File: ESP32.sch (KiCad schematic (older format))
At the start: 15 parts, among them J201 Conn_01x20, J202 Conn_01x20, U201 ESP32-WROOM-32D

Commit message: Rough PCB layout
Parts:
- removed J201, J202: Conn_01x20, symbol Connector_Generic:Conn_01x20
- added C203: 100nF, Capacitor_SMD:C_0402_1005Metric, symbol Device:C
- added J201: Conn_02x13_Odd_Even, Connector_PinHeader_2.54mm:PinHeader_2x13_P2.54mm_Vertical, symbol Connector_Generic:Conn_02x13_Odd_Even
- added J202: Conn_02x10_Odd_Even, Connector_PinHeader_2.54mm:PinHeader_2x10_P2.54mm_Vertical, symbol Connector_Generic:Conn_02x10_Odd_Even
- added J203: Conn_01x02, Connector_PinHeader_2.54mm:PinHeader_1x02_P2.54mm_Vertical, symbol Connector_Generic:Conn_01x02
- added R211, R212: 1k, Resistor_SMD:R_0402_1005Metric, symbol Device:R
- C201: value 100n -> 100nF; footprint (none) -> Capacitor_SMD:C_0402_1005Metric
- C202: footprint Capacitor_SMD:C_0805_2012Metric -> Capacitor_SMD:C_0603_1608Metric
- R201: footprint (none) -> Resistor_SMD:R_0402_1005Metric
- R202, R203, R204, R205, R206, R207, R208, R209, R210: footprint (none) -> Resistor_SMD:R_0603_1608Metric
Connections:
- net labels added: USB_5V
- net labels removed: EXT_5V, SCK, SCS, SDI, SDO, SHD, SWP
- wire segments 45 -> 53
- no-connect marks 0 -> 6
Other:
- moved on the sheet: C202, R201, U201

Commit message: Specified JLCPCB footprints for components
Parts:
- C201, C203: LCSC (none) -> C1525
- C202: LCSC C45783 -> C59461
- J201: LCSC (none) -> C358701
- J202: LCSC (none) -> C358699
- J203: LCSC (none) -> C376075
- R201: LCSC (none) -> C25744
- R202, R203, R204, R205, R206, R207, R208, R209, R210: LCSC (none) -> C21189
- R211, R212: LCSC (none) -> C11702
- U201: LCSC (none) -> C82899
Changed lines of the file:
@@
 F 2 "RF_Module:ESP32-WROOM-32" H 3700 1750 50  0001 C CNN
 F 3 "https://www.espressif.com/sites/default/files/documentation/esp32-wroom-32d_esp32-wroom-32u_datasheet_en.pdf" H 3400 3300 50  0001 C CNN
+F 4 "C82899" H 3700 3250 50  0001 C CNN "LCSC"
 	1    3700 3250
 	1    0    0    -1
@@
 F 3 "~" H 3350 1550 50  0001 C CNN
 F 4 "Min 6.3V" H 3350 1550 50  0001 C CNN "Notes"
-F 5 "C45783" H 3350 1550 50  0001 C CNN "LCSC"
+F 5 "C59461" H 3350 1550 50  0001 C CNN "LCSC"
 	1    3350 1550
 	-1   0    0    1
@@
 F 2 "Resistor_SMD:R_0402_1005Metric" V 1430 2400 50  0001 C CNN
 F 3 "~" H 1500 2400 50  0001 C CNN
+F 4 "C25744" H 1500 2400 50  0001 C CNN "LCSC"
 	1    1500 2400
 	1    0    0    -1
@@
 F 2 "Resistor_SMD:R_0603_1608Metric" V 8380 1800 50  0001 C CNN
 F 3 "~" H 8450 1800 50  0001 C CNN
+F 4 "C21189" H 8450 1800 50  0001 C CNN "LCSC"
 	1    8450 1800
 	0    -1   1    0
@@
 F 2 "Resistor_SMD:R_0603_1608Metric" V 8380 2000 50  0001 C CNN
 F 3 "~" H 8450 2000 50  0001 C CNN
+F 4 "C21189" H 8450 2000 50  0001 C CNN "LCSC"
 	1    8450 2000
 	0    -1   1    0
@@
 F 2 "Resistor_SMD:R_0603_1608Metric" V 8380 2650 50  0001 C CNN
 F 3 "~" H 8450 2650 50  0001 C CNN
+F 4 "C21189" H 8450 2650 50  0001 C CNN "LCSC"
 	1    8450 2650
 	0    1    1    0
@@
 F 2 "Resistor_SMD:R_0603_1608Metric" V 8380 2400 50  0001 C CNN
 F 3 "~" H 8450 2400 50  0001 C CNN
+F 4 "C21189" H 8450 2400 50  0001 C CNN "LCSC"
 	1    8450 2400
 	0    1    1    0
@@
 F 2 "Resistor_SMD:R_0603_1608Metric" V 8380 3750 50  0001 C CNN
 F 3 "~" H 8450 3750 50  0001 C CNN
+F 4 "C21189" H 8450 3750 50  0001 C CNN "LCSC"
 	1    8450 3750
 	0    1    1    0
@@
 F 2 "Resistor_SMD:R_0603_1608Metric" V 8380 4200 50  0001 C CNN
 F 3 "~" H 8450 4200 50  0001 C CNN
+F 4 "C21189" H 8450 4200 50  0001 C CNN "LCSC"
 	1    8450 4200
 	0    1    1    0
@@
 F 2 "Resistor_SMD:R_0603_1608Metric" V 8380 4400 50  0001 C CNN
 F 3 "~" H 8450 4400 50  0001 C CNN
+F 4 "C21189" H 8450 4400 50  0001 C CNN "LCSC"
 	1    8450 4400
 	0    1    1    0
@@
 F 2 "Resistor_SMD:R_0603_1608Metric" V 8380 3050 50  0001 C CNN
 F 3 "~" H 8450 3050 50  0001 C CNN
+F 4 "C21189" H 8450 3050 50  0001 C CNN "LCSC"
 	1    8450 3050
 	0    1    1    0
@@
 F 2 "Resistor_SMD:R_0603_1608Metric" V 8380 3300 50  0001 C CNN
 F 3 "~" H 8450 3300 50  0001 C CNN
+F 4 "C21189" H 8450 3300 50  0001 C CNN "LCSC"
 	1    8450 3300
 	0    1    1    0
@@
 F 2 "Resistor_SMD:R_0402_1005Metric" V 1530 3450 50  0001 C CNN
 F 3 "~" H 1600 3450 50  0001 C CNN
+F 4 "C11702" H 1600 3450 50  0001 C CNN "LCSC"
 	1    1600 3450
 	0    1    1    0
@@
 F 2 "Resistor_SMD:R_0402_1005Metric" V 1830 2600 50  0001 C CNN
 F 3 "~" H 1900 2600 50  0001 C CNN
+F 4 "C11702" H 1900 2600 50  0001 C CNN "LCSC"
 	1    1900 2600
 	0    1    1    0
@@
 F 2 "Capacitor_SMD:C_0402_1005Metric" H 1838 3450 50  0001 C CNN
 F 3 "~" H 1800 3600 50  0001 C CNN
+F 4 "C1525" H 1800 3600 50  0001 C CNN "LCSC"
 	1    1800 3600
 	1    0    0    -1
@@
 F 2 "Capacitor_SMD:C_0402_1005Metric" H 2188 2600 50  0001 C CNN
 F 3 "~" H 2150 2750 50  0001 C CNN
+F 4 "C1525" H 2150 2750 50  0001 C CNN "LCSC"
 	1    2150 2750
 	1    0    0    -1
@@
 F 2 "Connector_PinHeader_2.54mm:PinHeader_1x02_P2.54mm_Vertical" H 6150 5400 50  0001 C CNN
 F 3 "~" H 6150 5400 50  0001 C CNN
+F 4 "C376075" H 6150 5400 50  0001 C CNN "LCSC"
 	1    6150 5400
 	1    0    0    -1
@@
 F 2 "Connector_PinHeader_2.54mm:PinHeader_2x13_P2.54mm_Vertical" H 6150 2700 50  0001 C CNN
 F 3 "~" H 6150 2700 50  0001 C CNN
+F 4 "C358701" H 6150 2700 50  0001 C CNN "LCSC"
 	1    6150 2700
 	1    0    0    -1
@@
 F 2 "Connector_PinHeader_2.54mm:PinHeader_2x10_P2.54mm_Vertical" H 6150 4300 50  0001 C CNN
 F 3 "~" H 6150 4300 50  0001 C CNN
+F 4 "C358699" H 6150 4300 50  0001 C CNN "LCSC"
 	1    6150 4300
 	1    0    0    -1

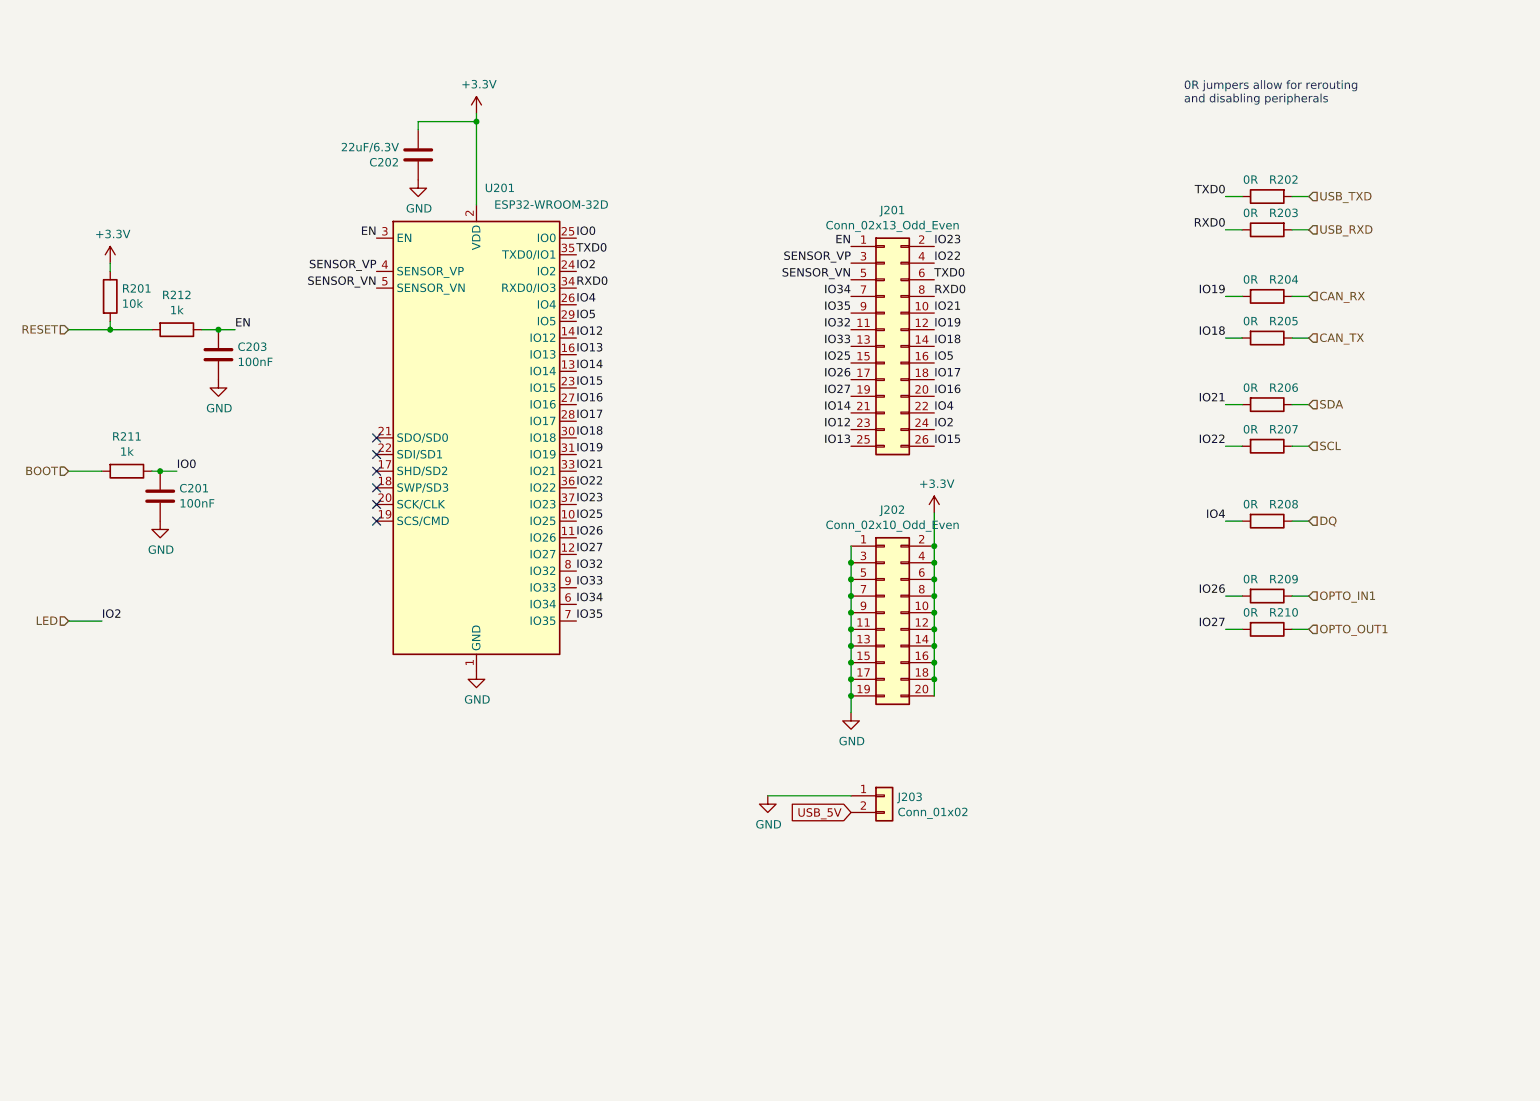
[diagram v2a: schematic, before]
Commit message: Added decoupling caps next to trace vias and copper fill islands
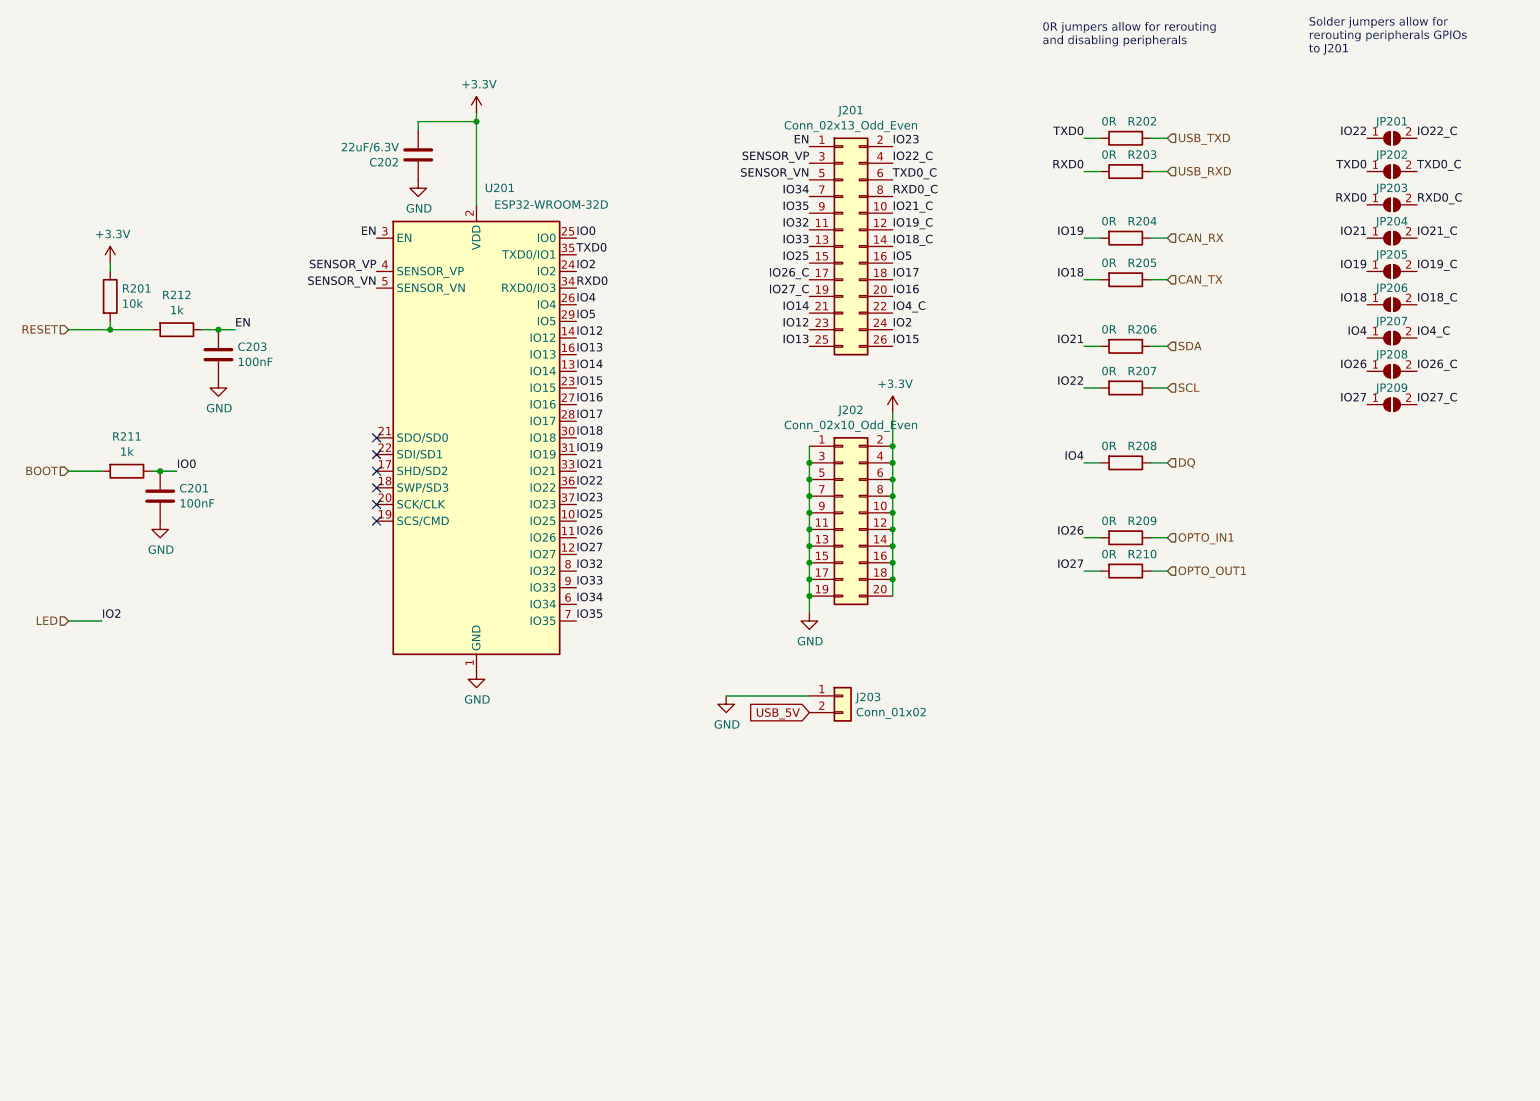
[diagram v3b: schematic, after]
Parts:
- added JP201, JP202, JP203, JP204, JP205, JP206, JP207, JP208, JP209: SolderJumper_2_Open, SH-ESP32:SolderJumper-2_P1.3mm_Open_TrianglePad_Narrow, symbol Jumper:SolderJumper_2_Open
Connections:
- net IO18: now also JP206.1 (A); no longer J201.14 (Pin_14)
- net IO19: now also JP205.1 (A); no longer J201.12 (Pin_12)
- net IO21: now also JP204.1 (A); no longer J201.10 (Pin_10)
- net IO22: now also JP201.1 (A); no longer J201.4 (Pin_4)
- net IO26: now also JP208.1 (A); no longer J201.17 (Pin_17)
- net IO27: now also JP209.1 (A); no longer J201.19 (Pin_19)
- net IO4: now also JP207.1 (A); no longer J201.22 (Pin_22)
- net RXD0: now also JP203.1 (A); no longer J201.8 (Pin_8)
- net TXD0: now also JP202.1 (A); no longer J201.6 (Pin_6)
- new net IO18_C: J201.14 (Pin_14), JP206.2 (B)
- new net IO19_C: J201.12 (Pin_12), JP205.2 (B)
- new net IO21_C: J201.10 (Pin_10), JP204.2 (B)
- new net IO22_C: J201.4 (Pin_4), JP201.2 (B)
- new net IO26_C: J201.17 (Pin_17), JP208.2 (B)
- new net IO27_C: J201.19 (Pin_19), JP209.2 (B)
- new net IO4_C: J201.22 (Pin_22), JP207.2 (B)
- new net RXD0_C: J201.8 (Pin_8), JP203.2 (B)
- new net TXD0_C: J201.6 (Pin_6), JP202.2 (B)
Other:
- note added: "Solder jumpers allow for \nrerouting peripherals GPIOs\nto J201"
- moved on the sheet: J201, J202, J203, R202, R203, R204, R205, R206, R207, R208, R209, R210
